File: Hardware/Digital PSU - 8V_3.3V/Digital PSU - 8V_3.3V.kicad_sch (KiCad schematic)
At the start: 16 parts, among them J6 ESP32 power, J7 Opt. 3V3 power, J8 DC in, J9 Relay power, U2 LM7808_TO220, U3 LD1117V33

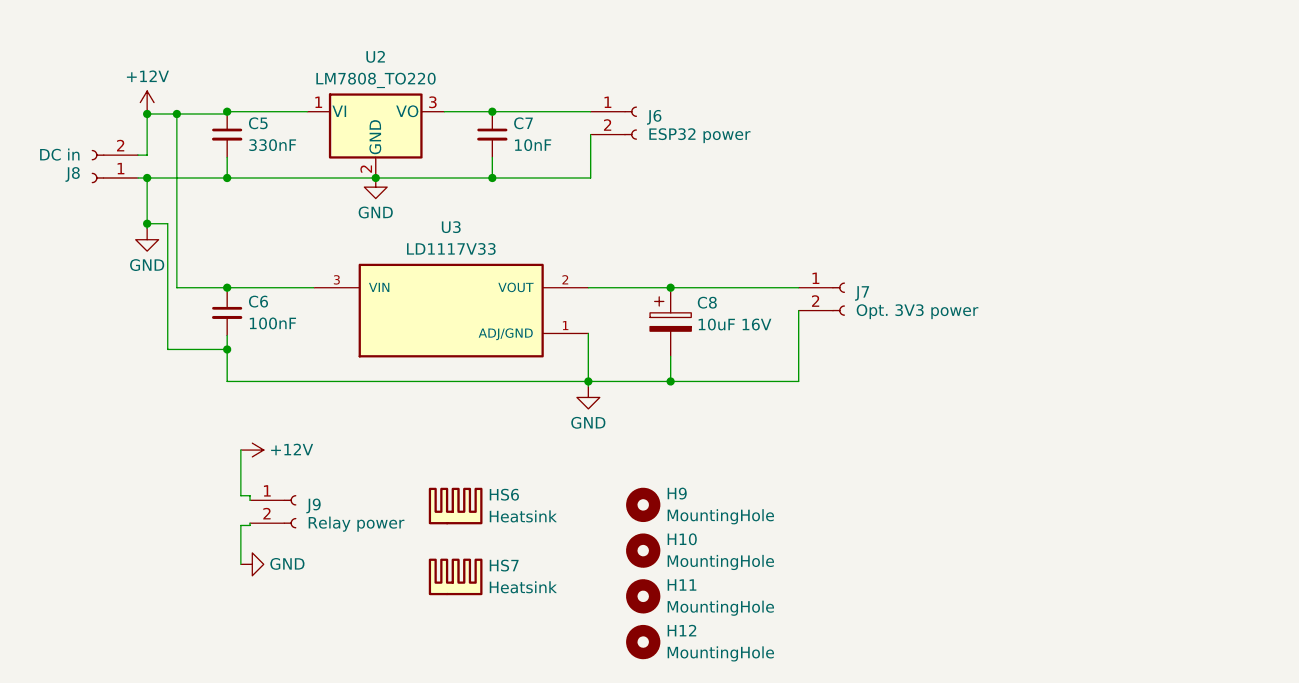
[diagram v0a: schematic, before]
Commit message: Updated pcb 3.3V + adjust of connectors on controller pcb
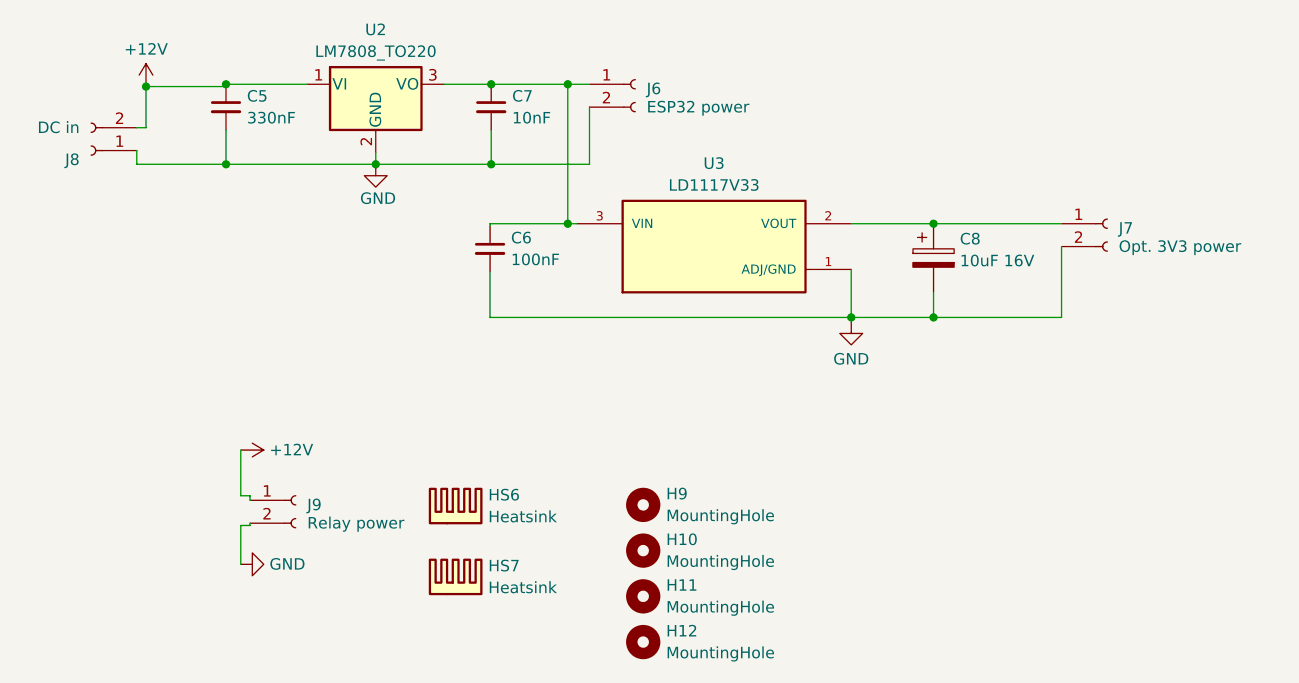
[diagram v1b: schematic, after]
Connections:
- net +12V: no longer C6.1, U3.3 (VIN)
- net at C7.1, J6.1 (Pin_1), U2.3 (VO): now also C6.1, U3.3 (VIN)
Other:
- moved on the sheet: C5, C6, C7, C8, J6, J7, J8, U2, U3
